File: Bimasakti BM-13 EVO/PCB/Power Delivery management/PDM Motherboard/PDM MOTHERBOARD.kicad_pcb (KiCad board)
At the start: 2 copper layers, 108 x 101.3 mm, 25 parts

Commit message: pdm jadi tapi arjun bakal ngerubah posisi pdm emang anjgg anak satu ini. sama pinnya juga mau dia ganti apalah itu ya allahh capek garap pdm
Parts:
- added N1: pdm 3.3V, Symbol:OSHW-Symbol_6.7x6mm_SilkScreen, F.Cu at (91.3, 39.7)
- added N2: pdm 5v, Symbol:OSHW-Symbol_6.7x6mm_SilkScreen, F.Cu at (91.3, 89.2)
- moved 12out1 47.2 mm to (81.6, 113.8)
- moved 3Vin1 27.0 mm to (112.9, 32.4)
- moved 5Vin1 18.6 mm to (113.7, 77.7)
- moved D4 18.2 mm to (118.6, 77.9)
- moved D5 13.9 mm to (116.2, 45.4)
- moved 12out2 11.6 mm to (81.2, 64.6)
- moved D6 7.64 mm to (116.3, 21.6), turned to 90 degrees
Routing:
- net +12: track 93.0 -> 162.8 mm
- net 3Vin: track 20.3 -> 34.9 mm
- net GND: track 51.3 -> 45.5 mm
- net 5Vin: track 41.0 -> 43.5 mm
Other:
- board size 108 x 101.3 mm -> 108 x 103.1 mm

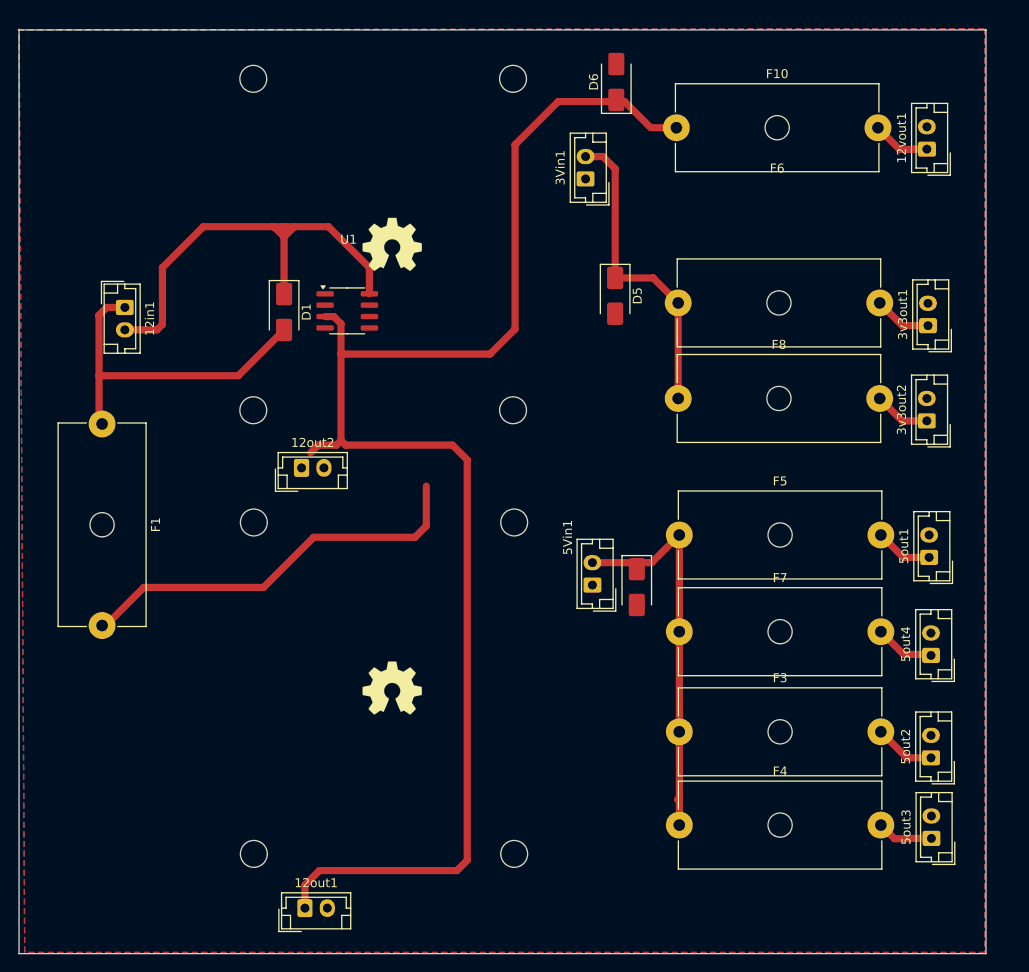
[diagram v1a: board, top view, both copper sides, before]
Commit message: pdm finishing tambah logo
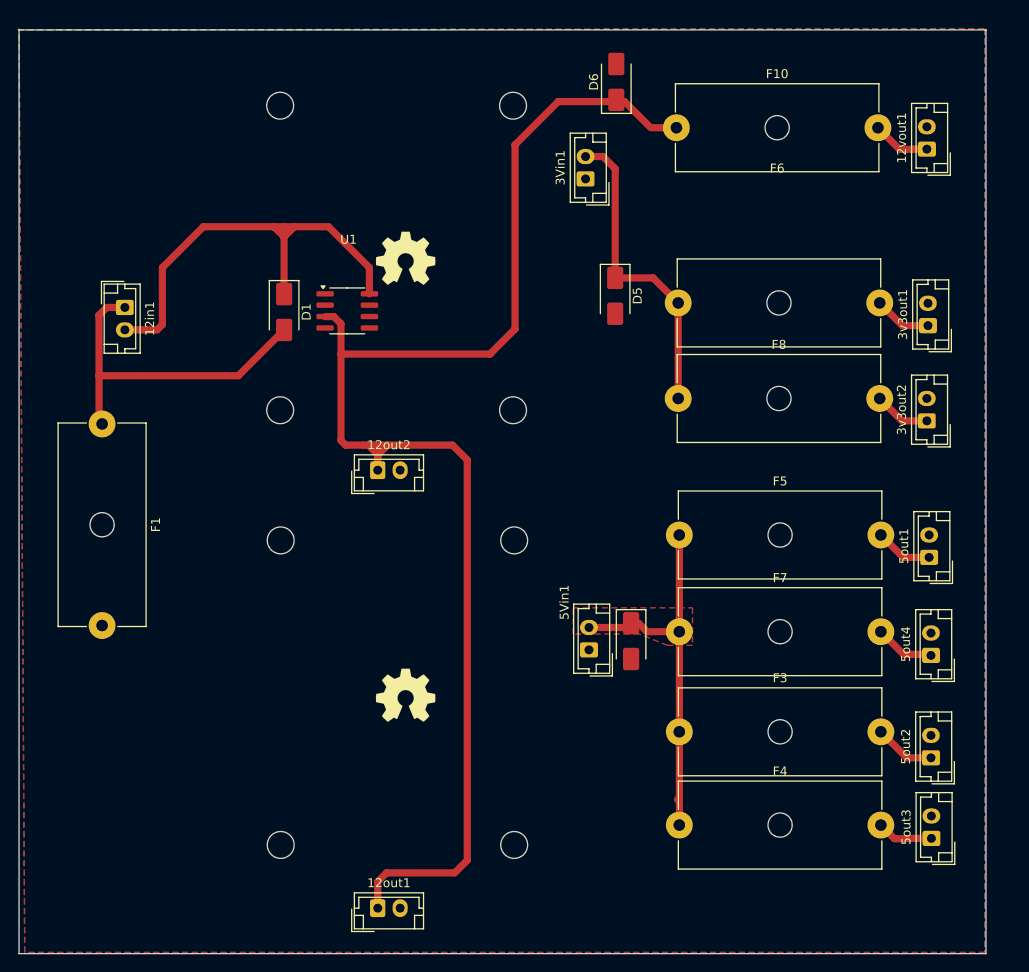
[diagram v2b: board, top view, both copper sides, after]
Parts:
- moved 12out2 8.51 mm to (89.7, 64.9)
- moved 12out1 8.13 mm to (89.7, 113.8)
- moved 5Vin1 7.25 mm to (113.3, 85.0)
- moved D4 6.07 mm to (118.0, 84.0)
- moved N1 2.16 mm to (92.8, 41.3)
- moved N2 1.70 mm to (92.8, 90.0)
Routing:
- net GND: track 45.5 -> 0.11 mm
- net +12: track 162.8 -> 157.3 mm
- net 5Vin: track 43.5 -> 42.5 mm
- added copper zone on F.Cu, net 5Vin
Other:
- outline, holes or cut-outs redrawn
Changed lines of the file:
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@@
 	(footprint "Symbol:OSHW-Symbol_6.7x6mm_SilkScreen"
 		(layer "F.Cu")
-		(at 91.307 89.239)
+		(at 92.807 90.039)
 		(descr "Open Source Hardware Symbol")
 		(tags "Logo Symbol OSHW")
@@
 	(footprint "Connector_JST:JST_EH_B2B-EH-A_1x02_P2.50mm_Vertical"
 		(layer "F.Cu")
-		(at 81.193 64.643)
+		(at 89.702 64.897)
 		(descr "JST EH series connector, B2B-EH-A (http://www.jst-mfg.com/product/pdf/eng/eEH.pdf), generated with kicad-footprint-generator")
 		(tags "connector JST EH vertical")
@@
 	(footprint "Connector_JST:JST_EH_B2B-EH-A_1x02_P2.50mm_Vertical"
 		(layer "F.Cu")
-		(at 81.574 113.792)
+		(at 89.702 113.792)
 		(descr "JST EH series connector, B2B-EH-A (http://www.jst-mfg.com/product/pdf/eng/eEH.pdf), generated with kicad-footprint-generator")
 		(tags "connector JST EH vertical")
@@
 	(footprint "Diode_SMD:D_SMA"
 		(layer "F.Cu")
-		(at 118.618 77.946 -90)
+		(at 117.983 83.979 -90)
 		(descr "Diode SMA (DO-214AC)")
 		(tags "Diode SMA (DO-214AC)")
@@
 	(footprint "Connector_JST:JST_EH_B2B-EH-A_1x02_P2.50mm_Vertical"
 		(layer "F.Cu")
-		(at 113.665 77.724 90)
+		(at 113.284 84.963 90)
 		(descr "JST EH series connector, B2B-EH-A (http://www.jst-mfg.com/product/pdf/eng/eEH.pdf), generated with kicad-footprint-generator")
 		(tags "connector JST EH vertical")
@@
 	(footprint "Symbol:OSHW-Symbol_6.7x6mm_SilkScreen"
 		(layer "F.Cu")
-		(at 91.307 39.709)
+		(at 92.807 41.259)
 		(descr "Open Source Hardware Symbol")
 		(tags "Logo Symbol OSHW")
@@
 	)
 	(gr_circle
-		(center 75.807 58.209)
-		(end 77.307 58.209)
+		(center 78.807 58.209)
+		(end 80.307 58.209)
 		(stroke
 			(width 0.05)
@@
 	)
 	(gr_circle
-		(center 104.934 107.739)
-		(end 106.434 107.739)
+		(center 104.934 106.739)
+		(end 106.434 106.739)
 		(stroke
 			(width 0.05)
@@
 	)
 	(gr_circle
-		(center 104.807 21.209)
-		(end 106.307 21.209)
+		(center 104.807 24.209)
+		(end 106.307 24.209)
 		(stroke
 			(width 0.05)
@@
 	)
 	(gr_circle
-		(center 104.934 70.739)
-		(end 106.434 70.739)
+		(center 104.934 72.739)
+		(end 106.434 72.739)
 		(stroke
 			(width 0.05)
@@
 	)
 	(gr_circle
-		(center 75.807 21.209)
-		(end 77.307 21.209)
+		(center 78.807 24.209)
+		(end 80.307 24.209)
 		(stroke
 			(width 0.05)
@@
 	)
 	(gr_circle
-		(center 75.869 107.739)
-		(end 77.369 107.739)
+		(center 78.869 106.739)
+		(end 80.369 106.739)
 		(stroke
 			(width 0.05)
@@
 	)
 	(gr_circle
-		(center 75.869 70.739)
-		(end 77.369 70.739)
+		(center 78.869 72.739)
+		(end 80.369 72.739)
 		(stroke
 			(width 0.05)
@@
 	)
 	(segment
-		(start 95.123 71.12)
-		(end 95.123 66.675)
-		(width 0.8)
-		(layer "F.Cu")
-		(net 2)
-	)
-	(segment
-		(start 93.853 72.39)
-		(end 95.123 71.12)
-		(width 0.8)
-		(layer "F.Cu")
-		(net 2)
-	)
-	(segment
 		(start 151.471 46.228)
 		(end 151.511 46.268)
@@
 	)
 	(segment
-		(start 76.952 77.988)
-		(end 82.55 72.39)
-		(width 0.8)
-		(layer "F.Cu")
-		(net 2)
-	)
-	(segment
-		(start 59.13 82.445)
-		(end 63.587 77.988)
-		(width 0.8)
-		(layer "F.Cu")
-		(net 2)
-	)
-	(segment
-		(start 63.587 77.988)
-		(end 76.952 77.988)
-		(width 0.8)
-		(layer "F.Cu")
-		(net 2)
-	)
-	(segment
-		(start 82.55 72.39)
-		(end 93.853 72.39)
-		(width 0.8)
-		(layer "F.Cu")
-		(net 2)
-	)
-	(segment
 		(start 151.852 94.107)
 		(end 151.892 94.147)
@@
 	)
 	(segment
-		(start 58.928 82.243)
-		(end 59.13 82.445)
-		(width 0.8)
-		(layer "F.Cu")
-		(net 2)
-	)
-	(segment
 		(start 88.773 42.291)
 		(end 84.201 37.719)
@@
 	)
 	(segment
-		(start 123.203 101.664)
-		(end 123.37 101.831)
+		(start 119.761 82.931)
+		(end 123.37 82.931)
+		(width 0.8)
+		(layer "F.Cu")
+		(net 5)
+	)
+	(segment
+		(start 117.499 82.463)
+		(end 113.284 82.463)
+		(width 0.8)
+		(layer "F.Cu")
+		(net 5)
+	)
+	(segment
+		(start 117.983 81.979)
+		(end 118.809 81.979)
 		(width 0.8)
 		(layer "F.Cu")
@@
 	(segment
 		(start 123.203 101.664)
-		(end 123.37 101.497)
+		(end 123.37 101.831)
 		(width 0.8)
 		(layer "F.Cu")
@@
 	)
 	(segment
-		(start 123.37 101.831)
-		(end 123.37 104.521)
+		(start 123.203 101.664)
+		(end 123.37 101.497)
 		(width 0.8)
 		(layer "F.Cu")
@@
 	)
 	(segment
-		(start 113.665 75.224)
-		(end 120.282 75.224)
+		(start 123.37 101.831)
+		(end 123.37 104.521)
 		(width 0.8)
 		(layer "F.Cu")
@@
 	)
 	(segment
-		(start 120.282 75.224)
-		(end 123.37 72.136)
+		(start 123.37 101.497)
+		(end 123.37 94.107)
 		(width 0.8)
 		(layer "F.Cu")
@@
 	)
 	(segment
-		(start 123.37 101.497)
-		(end 123.37 94.107)
+		(start 118.809 81.979)
+		(end 119.761 82.931)
 		(width 0.8)
 		(layer "F.Cu")
@@
 	)
 	(segment
-		(start 85.09 62.103)
-		(end 83.058 62.103)
+		(start 89.702 63.206)
+		(end 90.805 62.103)
 		(width 0.8)
 		(layer "F.Cu")
@@
 	)
 	(segment
-		(start 99.695 63.754)
+		(start 98.044 62.103)
+		(end 90.805 62.103)
+		(width 0.8)
+		(layer "F.Cu")
+		(net 10)
+	)
+	(segment
+		(start 86.106 62.103)
+		(end 88.138 62.103)
+		(width 0.8)
+		(layer "F.Cu")
+		(net 10)
+	)
+	(segment
+		(start 98.298 109.855)
 		(end 99.695 108.458)
 		(width 0.8)
@@
 	)
 	(segment
+		(start 88.138 62.103)
+		(end 88.646 62.103)
+		(width 0.8)
+		(layer "F.Cu")
+		(net 10)
+	)
+	(segment
+		(start 89.702 64.897)
+		(end 89.702 63.667)
+		(width 0.8)
+		(layer "F.Cu")
+		(net 10)
+	)
+	(segment
 		(start 105.029 28.575)
 		(end 109.855 23.749)
@@
 	)
 	(segment
+		(start 89.702 110.831)
+		(end 90.678 109.855)
+		(width 0.8)
+		(layer "F.Cu")
+		(net 10)
+	)
+	(segment
+		(start 89.702 113.792)
+		(end 89.702 110.831)
+		(width 0.8)
+		(layer "F.Cu")
+		(net 10)
+	)
+	(segment
+		(start 89.702 63.206)
+		(end 89.702 62.397)
+		(width 0.8)
+		(layer "F.Cu")
+		(net 10)
+	)
+	(segment
+		(start 89.702 63.206)
+		(end 89.702 63.159)
+		(width 0.8)
+		(layer "F.Cu")
+		(net 10)
+	)
+	(segment
+		(start 89.448 62.143)
+		(end 89.408 62.103)
+		(width 0.2)
+		(layer "F.Cu")
+		(net 10)
+	)
+	(segment
 		(start 109.855 23.749)
 		(end 117.253 23.749)
@@
 	)
 	(segment
-		(start 99.695 108.458)
-		(end 98.552 109.601)
+		(start 89.702 63.159)
+		(end 88.646 62.103)
 		(width 0.8)
 		(layer "F.Cu")
@@
 	)
 	(segment
-		(start 83.058 62.103)
-		(end 82.209 62.952)
+		(start 88.9 62.103)
+		(end 89.408 62.103)
 		(width 0.8)
 		(layer "F.Cu")
@@
 	)
 	(segment
-		(start 98.044 62.103)
-		(end 99.695 63.754)
+		(start 89.702 63.667)
+		(end 89.702 63.206)
 		(width 0.8)
 		(layer "F.Cu")
@@
 	)
 	(segment
-		(start 85.598 61.595)
-		(end 85.09 62.103)
+		(start 88.646 62.103)
+		(end 88.9 62.103)
 		(width 0.8)
 		(layer "F.Cu")
@@
 	)
 	(segment
+		(start 89.702 63.667)
+		(end 89.702 62.905)
+		(width 0.8)
+		(layer "F.Cu")
+		(net 10)
+	)
+	(segment
 		(start 117.253 23.749)
 		(end 120.174 26.67)
@@
 	)
 	(segment
-		(start 81.574 111.212)
-		(end 81.574 113.792)
+		(start 99.695 63.754)
+		(end 98.044 62.103)
 		(width 0.8)
 		(layer "F.Cu")
@@
 	)
 	(segment
-		(start 86.106 62.103)
-		(end 98.044 62.103)
+		(start 89.408 62.103)
+		(end 90.805 62.103)
 		(width 0.8)
 		(layer "F.Cu")
@@
 	)
 	(segment
-		(start 98.552 109.601)
-		(end 83.185 109.601)
+		(start 99.695 108.458)
+		(end 99.695 63.754)
 		(width 0.8)
 		(layer "F.Cu")
@@
 	)
 	(segment
-		(start 83.185 109.601)
-		(end 81.574 111.212)
+		(start 90.678 109.855)
+		(end 98.298 109.855)
 		(width 0.8)
 		(layer "F.Cu")
@@
 	)
 	(zone
+		(net 5)
+		(net_name "5Vin")
+		(layer "F.Cu")
+		(hatch edge 0.5)
+		(priority 1)
+		(connect_pads yes
+			(clearance 0.5)
+		)
+		(min_thickness 0.25)
+		(filled_areas_thickness no)
+		(fill yes
+			(thermal_gap 0.5)
+			(thermal_bridge_width 0.5)
+		)
+		(polygon
+			(pts
+				(xy 111.506 80.264) (xy 124.841 80.264) (xy 124.841 84.455) (xy 122.047 84.455) (xy 118.872 83.185)
+				(xy 111.506 83.185)
+			)
+		)
+	)
+	(zone

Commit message: cicil assembly
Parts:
- added G***: LOGO, 0_logo:logo_22x15.3, F.Cu at (62.5, 95.0)
- added H1: MountingHole_Pad, MountingHole:MountingHole_3.2mm_M3_ISO7380_Pad_TopBottom, F.Cu at (153.4, 19.4)
- added H2: MountingHole_Pad, MountingHole:MountingHole_3.2mm_M3_ISO7380_Pad_TopBottom, F.Cu at (153.4, 114.2)
- added H3: MountingHole_Pad, MountingHole:MountingHole_3.2mm_M3_ISO7380_Pad_TopBottom, F.Cu at (53.9, 114.2)
- added H4: MountingHole_Pad, MountingHole:MountingHole_3.2mm_M3_ISO7380_Pad_TopBottom, F.Cu at (53.9, 19.4)
- moved U1 16.1 mm to (70.3, 38.9)
- moved D1 13.0 mm to (69.1, 39.1), turned to 90 degrees
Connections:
- 12in1 pad 1: Net-(12in1-Pin_1) -> GND
- D1 pad 2: Net-(12in1-Pin_1) -> GND
- F1 pad 1: Net-(12in1-Pin_1) -> GND
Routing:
- net Net-(12in1-Pin_1): track 38.6 -> 0.00 mm
- net Net-(12in1-Pin_2): track 51.5 -> 18.7 mm
- net +12: track 157.3 -> 179.6 mm
- net GND: track 0.11 -> 16.0 mm
- net 3Vin: track 34.9 -> 35.6 mm
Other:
- board size 108 x 103.1 mm -> 107.9 x 103.1 mm
- board text added: "PCB POWER DELIVERY MANAGEMENT"

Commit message: ngecilin pdm
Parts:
- removed 12out1, 12out2, 3Vin1, 5Vin1: ~, Connector_JST:JST_EH_B2B-EH-A_1x02_P2.50mm_Vertical
- removed F1, F10: 1A, Fuse:Fuseholder_Cylinder-5x20mm_Schurter_0031_8201_Horizontal_Open
- removed N1: pdm 3.3V, Symbol:OSHW-Symbol_6.7x6mm_SilkScreen
- removed N2: pdm 5v, Symbol:OSHW-Symbol_6.7x6mm_SilkScreen
- added F2: 3557-2, 0_FUSE:0_FUSE_3557-2, F.Cu at (134.7, 37.1)
- added F9: 3557-2, 0_FUSE:0_FUSE_3557-2, F.Cu at (82.6, 41.8)
- added U2: ~, BIMS_BUCK:BIMS_BUCK, F.Cu at (102.3, 22.0)
- added U3: ~, BIMS_BUCK:BIMS_BUCK, F.Cu at (102.3, 52.7)
- 12in1: footprint Connector_JST:JST_EH_B2B-EH-A_1x02_P2.50mm_Vertical -> TerminalBlock_TE-Connectivity:TerminalBlock_TE_282834-2_1x02_P2.54mm_Horizontal
- F3, F4, F5, F6, F7, F8: value 1A -> 3557-2; footprint Fuse:Fuseholder_Cylinder-5x20mm_Schurter_0031_8201_Horizontal_Open -> 0_FUSE:0_FUSE_3557-2
- moved F7 56.5 mm to (134.7, 27.6)
- moved F3 50.7 mm to (134.7, 44.7)
- moved F4 46.3 mm to (134.7, 59.6)
- moved F6 32.1 mm to (134.7, 76.2)
- moved 5out3 31.8 mm to (151.9, 74.2), turned to -90 degrees
- moved F8 31.2 mm to (135.1, 85.7)
- moved H3 30.7 mm to (75.3, 92.2)
- moved G*** 29.5 mm to (79.8, 71.1), turned to -90 degrees
- moved 12in1 22.4 mm to (82.3, 54.9)
- moved H2 21.8 mm to (153.4, 92.3)
- moved H4 21.5 mm to (75.3, 19.3)
- moved D1 21.2 mm to (82.8, 22.9), turned to 0 degrees
- moved 5out4 20.0 mm to (151.9, 65.6), turned to -90 degrees
- moved 5out1 17.7 mm to (151.9, 56.9), turned to -90 degrees
- moved 5out2 14.2 mm to (151.9, 82.8), turned to -90 degrees
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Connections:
- U1 pad 1: Net-(12in1-Pin_2) -> Net-(U1-D)
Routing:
- net +12: track 179.6 -> 104.4 mm
- net GND: track 16.0 -> 49.9 mm
- net Net-(12in1-Pin_2): track 18.7 -> 41.4 mm
- net Net-(5out2-Pin_1): track 6.80 -> 27.5 mm
- net 5Vin: track 42.5 -> 61.8 mm
- net Net-(3v3out2-Pin_1): track 6.30 -> 20.1 mm
- net Net-(3v3out1-Pin_1): track 6.44 -> 19.6 mm
- net Net-(U1-D): track 0.00 -> 12.6 mm
- net Net-(5out4-Pin_1): track 6.69 -> 18.2 mm
- net 3Vin: track 35.6 -> 46.0 mm
- net Net-(12vout1-Pin_1): track 6.48 -> 16.6 mm
- net Net-(5out1-Pin_1): track 6.42 -> 14.6 mm
- net Net-(5out3-Pin_1): track 6.29 -> 14.0 mm
- added copper zone on F.Cu, net 3Vin
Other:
- board size 107.9 x 103.1 mm -> 86.5 x 81.4 mm
- board text added: "3V3 board"
- board text added: "5V board"
- board text added: "semoga <10mVpp"
